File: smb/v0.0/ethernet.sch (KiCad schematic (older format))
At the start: 22 parts, among them J401 HR911105_RJ45, U201 ENC28J60, U301 74HC08, X201 25MHz

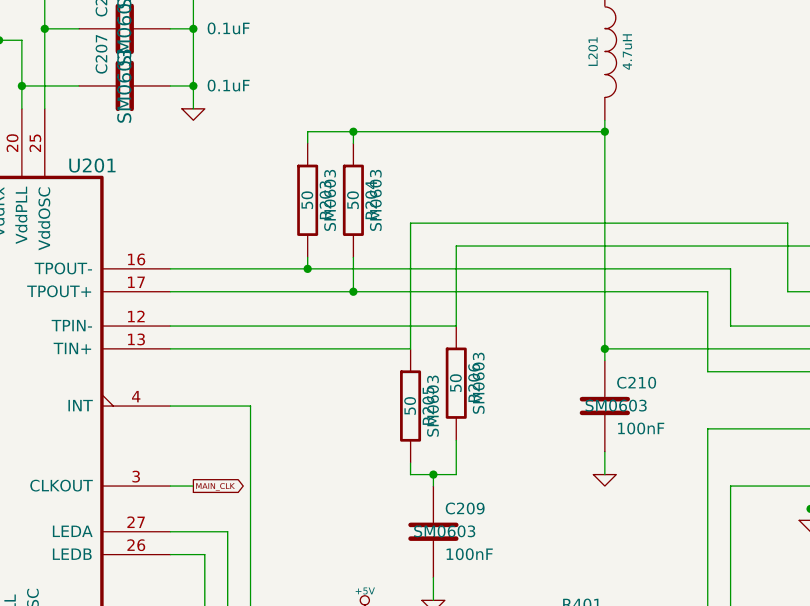
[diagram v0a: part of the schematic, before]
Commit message: Corrected production mistakes. SPI_CLK for ISP, MISO sdcard
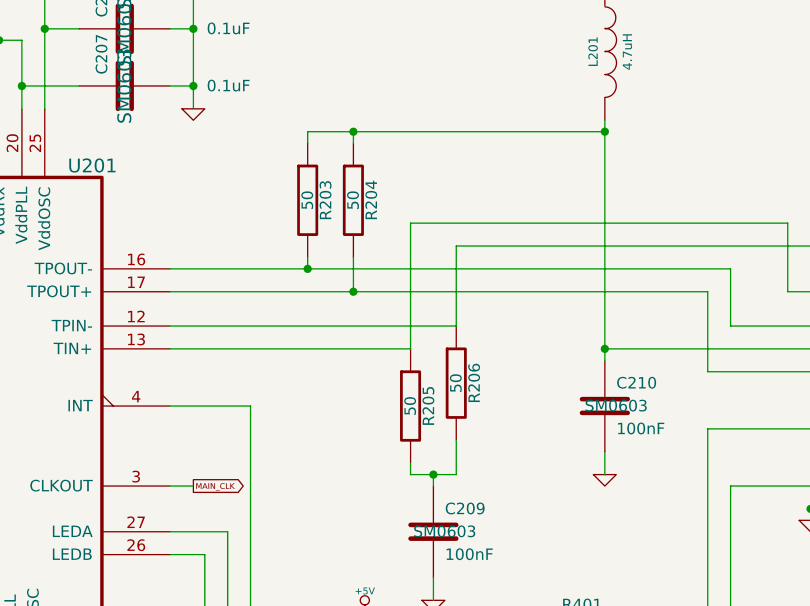
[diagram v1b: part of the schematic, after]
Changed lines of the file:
@@
-EESchema Schematic File Version 2  date jeu. 13 sept. 2012 22:24:34 CEST
+EESchema Schematic File Version 2  date 10/02/2013 13:01:35
 LIBS:power
 LIBS:device
@@
 EELAYER 25  0
 EELAYER END
-$Descr A4 11693 8268
+$Descr A4 11700 8267
 encoding utf-8
 Sheet 4 4
 Title "Short Main Board - SMB controler"
-Date "10 sep 2012"
+Date "10 feb 2013"
 Rev "0"
 Comp "XPLDUINO project"
@@
 F 0 "R204" V 7530 2500 50  0000 C CNN
 F 1 "50" V 7450 2500 50  0000 C CNN
-F 2 "SM0603" V 7550 2500 50  0000 C CNN
+F 2 "SM0603" V 7550 2500 50  0001 C CNN
 	1    7450 2500
 	1    0    0    -1
@@
 F 0 "R203" V 7330 2500 50  0000 C CNN
 F 1 "50" V 7250 2500 50  0000 C CNN
-F 2 "SM0603" V 7350 2500 50  0000 C CNN
+F 2 "SM0603" V 7350 2500 50  0001 C CNN
 	1    7250 2500
 	1    0    0    -1
@@
 F 0 "R206" V 7980 3300 50  0000 C CNN
 F 1 "50" V 7900 3300 50  0000 C CNN
-F 2 "SM0603" V 8000 3300 50  0000 C CNN
+F 2 "SM0603" V 8000 3300 50  0001 C CNN
 	1    7900 3300
 	1    0    0    -1
@@
 F 0 "R205" V 7780 3400 50  0000 C CNN
 F 1 "50" V 7700 3400 50  0000 C CNN
-F 2 "SM0603" V 7800 3400 50  0000 C CNN
+F 2 "SM0603" V 7800 3400 50  0001 C CNN
 	1    7700 3400
 	1    0    0    -1
